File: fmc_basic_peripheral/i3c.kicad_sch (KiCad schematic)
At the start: 4 parts, among them U25 MMC5603NJ

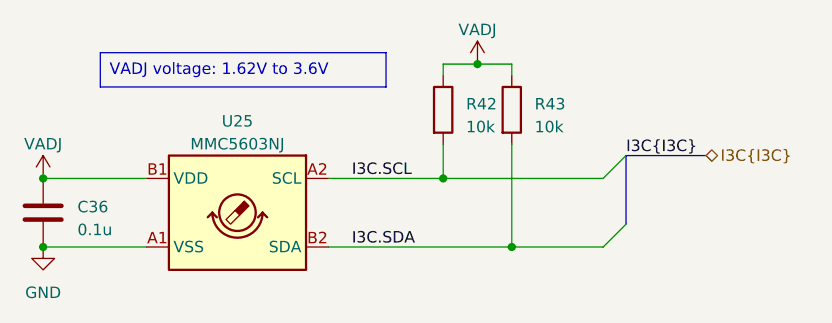
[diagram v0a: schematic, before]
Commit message: fmc_basic_peripheral: update library and preserve schematic connections
Signed-off-by: Huang Rui <vowstar@gmail.com>
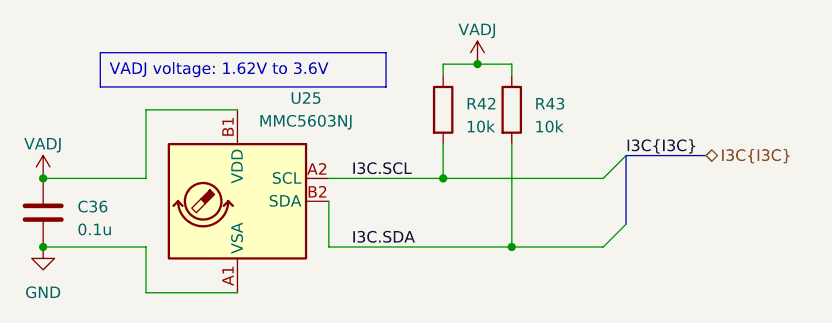
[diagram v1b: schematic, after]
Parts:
- U25: footprint CHIPSAlliance_Sensor:WLP4_N40P2X2_80X80X52N -> CHIPSAlliance_Sensor:WLCSP-4_0.8x0.8mm_Layout2x2_P0.4mm_Ball0.22mm_Pad0.25mm_NSMD
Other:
- moved on the sheet: U25
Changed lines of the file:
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@@
 	(symbol
 		(lib_id "CHIPSAlliance_Sensor:MMC5603NJ")
-		(at 124.46 72.39 0)
+		(at 116.84 77.47 0)
 		(mirror y)
 		(unit 1)
@@
 		(fields_autoplaced yes)
 		(property "Reference" "U25"
-			(at 116.84 68.58 0)
+			(at 124.46 66.04 0)
 			(effects
 				(font
@@
 		)
 		(property "Value" "MMC5603NJ"
-			(at 116.84 71.12 0)
+			(at 124.46 68.58 0)
 			(effects
 				(font
@@
 			)
 		)
-		(property "Footprint" "CHIPSAlliance_Sensor:WLP4_N40P2X2_80X80X52N"
+		(property "Footprint" "CHIPSAlliance_Sensor:WLCSP-4_0.8x0.8mm_Layout2x2_P0.4mm_Ball0.22mm_Pad0.25mm_NSMD"
 			(at 116.84 86.36 0)
 			(effects
@@
 		)
 	)
+	(wire (pts (xy 106.68 82.55) (xy 106.68 87.63)) (stroke (width 0) (type default)))
+	(wire (pts (xy 106.68 87.63) (xy 116.84 87.63)) (stroke (width 0) (type default)))
+	(wire (pts (xy 106.68 74.93) (xy 106.68 67.31)) (stroke (width 0) (type default)))
+	(wire (pts (xy 106.68 67.31) (xy 116.84 67.31)) (stroke (width 0) (type default)))
+	(wire (pts (xy 127 82.55) (xy 127 77.47)) (stroke (width 0) (type default)))
 )
